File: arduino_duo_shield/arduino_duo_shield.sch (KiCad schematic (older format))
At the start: 19 parts, among them J2 Spindle_Control, J3 Motor_Control, J4 Limit_Switches, J5 Spindle_Relay_Power, J6 Spindle_Signal, P1 CONN_01X01, P10 Digital, P11 PWM, P12 PWM, P13 Communication, P2 CONN_01X01, P3 CONN_01X01, P4 CONN_01X01, P5 CONN_01X01, P6 CONN_01X01, P7 Power, P8 Analog, P9 Analog, SW1 SW_Push

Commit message: Add signal mirror and control jumpers
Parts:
- removed J2: Spindle_Control, Connector_PinHeader_2.54mm:PinHeader_1x04_P2.54mm_Vertical, symbol Connector:Conn_01x04_Male
- removed J5: Spindle_Relay_Power, TerminalBlock:TerminalBlock_bornier-2_P5.08mm, symbol Connector:Conn_01x02_Female
- removed J6: Spindle_Signal, TerminalBlock:TerminalBlock_bornier-2_P5.08mm, symbol Connector:Conn_01x02_Female
- added J2: EStop, TerminalBlock:TerminalBlock_bornier-2_P5.08mm, symbol Connector:Conn_01x02_Male
- added J5: inverter_freq, TerminalBlock:TerminalBlock_bornier-2_P5.08mm, symbol Connector:Conn_01x02_Male
- added J6: inverter_cmd, TerminalBlock:TerminalBlock_bornier-2_P5.08mm, symbol Connector:Conn_01x02_Male
- added J8: inverter_power, TerminalBlock:TerminalBlock_bornier-2_P5.08mm, symbol Connector:Conn_01x02_Male
- added J9: Motor_Control_Mirror, Connector_PinHeader_2.54mm:PinHeader_2x12_P2.54mm_Vertical, symbol Connector_Generic:Conn_02x12_Odd_Even
- J4: footprint Connector_PinHeader_2.54mm:PinHeader_2x07_P2.54mm_Vertical -> Connector_PinHeader_2.54mm:PinHeader_2x09_P2.54mm_Vertical; symbol Connector_Generic:Conn_01x14 -> Connector_Generic:Conn_01x18
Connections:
- net labels added: Amn, Amx, spdir
- wire segments 199 -> 275
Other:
- moved on the sheet: J3, SW1

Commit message: Route all paths
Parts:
- removed P1, P2, P3, P4, P5, P6: CONN_01X01, Socket_Arduino_Mega:Arduino_1pin, symbol Connector_Generic:Conn_01x01
- J2: symbol Connector:Conn_01x02_Male -> Connector:Conn_01x02_Female
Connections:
- net Spindle_VFD_Control/inverter_frequency_10V: now also J5.1 (Pin_1)
- no-connect marks 62 -> 53
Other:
- note removed: "Holes"
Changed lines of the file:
@@
 $Descr A4 11693 8268
 encoding utf-8
-Sheet 1 5
+Sheet 1 4
 Title ""
 Date "mar. 31 mars 2015"
@@
 Text Label 3000 2300 0    60   ~ 0
 AREF
-Text Notes 1600 7400 0    60   ~ 0
-Holes
-$Comp
-L Connector_Generic:Conn_01x01 P1
-U 1 1 56D70B71
-P 1500 7050
-F 0 "P1" V 1600 7050 31  0000 C CNN
-F 1 "CONN_01X01" V 1600 7050 50  0001 C CNN
-F 2 "Socket_Arduino_Mega:Arduino_1pin" H 1500 7050 50  0001 C CNN
-F 3 "" H 1500 7050 50  0000 C CNN
-	1    1500 7050
-	0    -1   -1   0
-$EndComp
-$Comp
-L Connector_Generic:Conn_01x01 P2
-U 1 1 56D70C9B
-P 1600 7050
-F 0 "P2" V 1700 7050 31  0000 C CNN
-F 1 "CONN_01X01" V 1700 7050 50  0001 C CNN
-F 2 "Socket_Arduino_Mega:Arduino_1pin" H 1600 7050 50  0001 C CNN
-F 3 "" H 1600 7050 50  0000 C CNN
-	1    1600 7050
-	0    -1   -1   0
-$EndComp
-$Comp
-L Connector_Generic:Conn_01x01 P3
-U 1 1 56D70CE6
-P 1700 7050
-F 0 "P3" V 1800 7050 31  0000 C CNN
-F 1 "CONN_01X01" V 1800 7050 50  0001 C CNN
-F 2 "Socket_Arduino_Mega:Arduino_1pin" H 1700 7050 50  0001 C CNN
-F 3 "" H 1700 7050 50  0000 C CNN
-	1    1700 7050
-	0    -1   -1   0
-$EndComp
-$Comp
-L Connector_Generic:Conn_01x01 P4
-U 1 1 56D70D2C
-P 1800 7050
-F 0 "P4" V 1900 7050 31  0000 C CNN
-F 1 "CONN_01X01" V 1900 7050 50  0001 C CNN
-F 2 "Socket_Arduino_Mega:Arduino_1pin" H 1800 7050 50  0001 C CNN
-F 3 "" H 1800 7050 50  0000 C CNN
-	1    1800 7050
-	0    -1   -1   0
-$EndComp
-$Comp
-L Connector_Generic:Conn_01x01 P5
-U 1 1 56D711A2
-P 1900 7050
-F 0 "P5" V 2000 7050 31  0000 C CNN
-F 1 "CONN_01X01" V 2000 7050 50  0001 C CNN
-F 2 "Socket_Arduino_Mega:Arduino_1pin" H 1900 7050 50  0001 C CNN
-F 3 "" H 1900 7050 50  0000 C CNN
-	1    1900 7050
-	0    -1   -1   0
-$EndComp
-$Comp
-L Connector_Generic:Conn_01x01 P6
-U 1 1 56D711F0
-P 2000 7050
-F 0 "P6" V 2100 7050 31  0000 C CNN
-F 1 "CONN_01X01" V 2100 7050 50  0001 C CNN
-F 2 "Socket_Arduino_Mega:Arduino_1pin" H 2000 7050 50  0001 C CNN
-F 3 "" H 2000 7050 50  0000 C CNN
-	1    2000 7050
-	0    -1   -1   0
-$EndComp
-NoConn ~ 1500 7250
-NoConn ~ 1600 7250
-NoConn ~ 1700 7250
-NoConn ~ 1800 7250
-NoConn ~ 1900 7250
-NoConn ~ 2000 7250
 $Comp
 L conn_01x08_arduino_power:Conn_01x08_arduino_power P7
@@
 $EndComp
 Wire Wire Line
-	7800 5550 8150 5550
-Wire Wire Line
 	5100 5900 4350 5900
 Wire Wire Line
@@
 Text Label 4100 1250 0    50   ~ 0
 VREF+
-$Sheet
-S 8150 5350 750  500
-U 5D7DFDC0
-F0 "Spindle_Power_Control" 50
-F1 "Spindle_Power_Control.sch" 50
-F2 "ext_gnd" I L 8150 5750 50
-F3 "ext_sppwm" I L 8150 5550 50
-F4 "ext_vcc" I L 8150 5650 50
-F5 "ext_spenab" I L 8150 5450 50
-$EndSheet
 Wire Wire Line
 	4350 1250 6900 1250
@@
 Wire Wire Line
 	4350 5800 4350 1250
-Wire Wire Line
-	7800 5450 8150 5450
 Wire Wire Line
 	1700 1250 4350 1250
@@
 Wire Wire Line
 	1200 3050 1850 3050
-Wire Wire Line
-	1200 2500 1950 2500
 $Comp
 L power:PWR_FLAG #FLG0104
@@
 Wire Wire Line
 	11100 5950 11100 6200
-Connection ~ 1950 2500
-Wire Wire Line
-	1950 2500 2200 2500
 Wire Wire Line
 	1850 3050 2100 3050
 $Comp
-L Connector:Conn_01x02_Male J2
+L Connector:Conn_01x02_Female J2
 U 1 1 5E163504
 P 750 3300
-F 0 "J2" V 904 3112 50  0000 R CNN
-F 1 "EStop" V 813 3112 50  0000 R CNN
+F 0 "J2" V 750 3150 50  0000 R CNN
+F 1 "EStop" V 650 3150 50  0000 R CNN
 F 2 "TerminalBlock:TerminalBlock_bornier-2_P5.08mm" H 750 3300 50  0001 C CNN
 F 3 "~" H 750 3300 50  0001 C CNN
 	1    750  3300
-	0    -1   -1   0
+	0    -1   1    0
 $EndComp
 Wire Wire Line
@@
 	6600 5450 6850 5450
 Wire Wire Line
-	6600 5350 6850 5350
+	6600 5350 6750 5350
 Wire Wire Line
 	6600 5550 6850 5550
-NoConn ~ 6850 5250
 $Comp
 L Connector:Conn_01x02_Male J?
@@
 Wire Wire Line
 	6700 3900 7000 3900
-NoConn ~ 7800 5450
-NoConn ~ 7800 5550
+Wire Wire Line
+	1200 2500 1950 2500
+Wire Wire Line
+	6850 5250 6750 5250
+Wire Wire Line
+	6750 5250 6750 5350
+Connection ~ 6750 5350
+Wire Wire Line
+	6750 5350 6850 5350
 $EndSCHEMATC

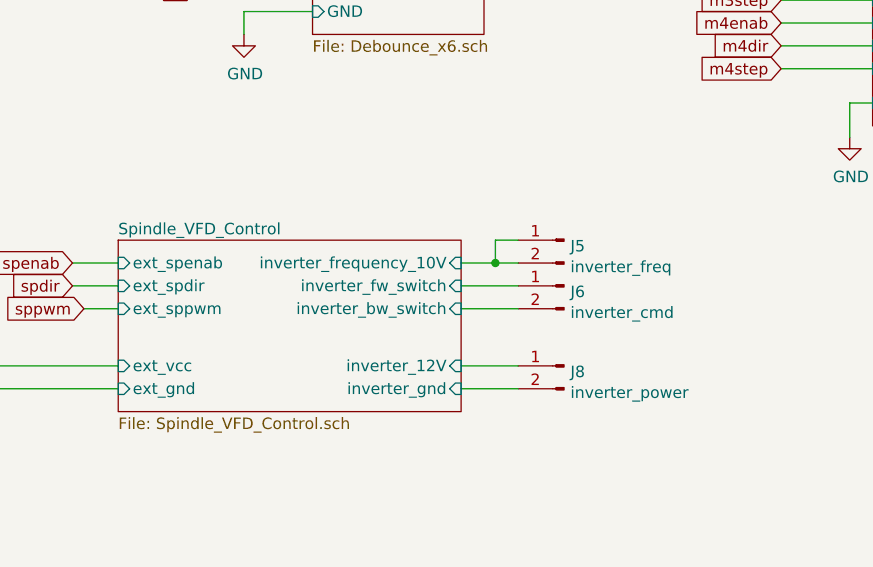
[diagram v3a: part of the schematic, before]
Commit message: Expose raw analog frequency control
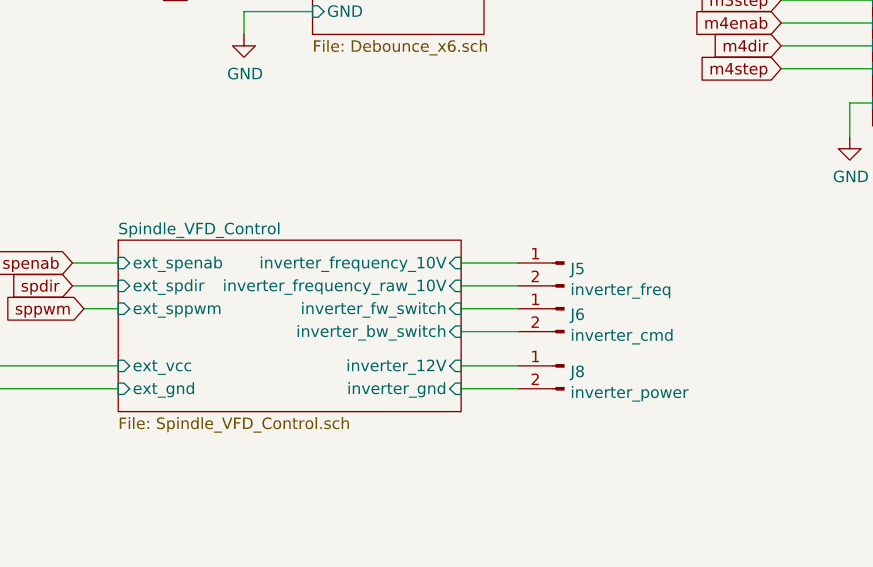
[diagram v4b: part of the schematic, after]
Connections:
- net Spindle_VFD_Control/inverter_frequency_10V: no longer J5.2 (Pin_2)
- new net Spindle_VFD_Control/inverter_frequency_raw_10V: J5.2 (Pin_2)
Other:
- moved on the sheet: J5, J6
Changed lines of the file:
@@
 F7 "ext_vcc" I L 5100 5800 50
 F8 "ext_spenab" I L 5100 5350 50
-F9 "inverter_fw_switch" I R 6600 5450 50
-F10 "inverter_bw_switch" I R 6600 5550 50
+F9 "inverter_fw_switch" I R 6600 5550 50
+F10 "inverter_bw_switch" I R 6600 5650 50
 F11 "inverter_gnd" I R 6600 5900 50
+F12 "inverter_frequency_raw_10V" I R 6600 5450 50
 $EndSheet
 Text GLabel 3450 2500 2    50   Output ~ 0
@@
 $EndComp
 Wire Wire Line
-	6600 5450 6850 5450
-Wire Wire Line
-	6600 5350 6750 5350
-Wire Wire Line
 	6600 5550 6850 5550
+Wire Wire Line
+	6600 5650 6850 5650
 $Comp
 L Connector:Conn_01x02_Male J?
 U 1 1 5E2CBC81
-P 7050 5250
+P 7050 5350
 AR Path="/5D7DFDC0/5E2CBC81" Ref="J?"  Part="1"
 AR Path="/5E2CBC81" Ref="J5"  Part="1"
-F 0 "J5" H 7022 5224 50  0000 R CNN
-F 1 "inverter_freq" H 7022 5133 50  0000 R CNN
-F 2 "TerminalBlock:TerminalBlock_bornier-2_P5.08mm" H 7050 5250 50  0001 C CNN
-F 3 "~" H 7050 5250 50  0001 C CNN
-	1    7050 5250
+F 0 "J5" H 7022 5324 50  0000 R CNN
+F 1 "inverter_freq" H 7022 5233 50  0000 R CNN
+F 2 "TerminalBlock:TerminalBlock_bornier-2_P5.08mm" H 7050 5350 50  0001 C CNN
+F 3 "~" H 7050 5350 50  0001 C CNN
+	1    7050 5350
 	-1   0    0    -1
 $EndComp
@@
 L Connector:Conn_01x02_Male J?
 U 1 1 5E2B9818
-P 7050 5450
+P 7050 5550
 AR Path="/5D7DFDC0/5E2B9818" Ref="J?"  Part="1"
 AR Path="/5E2B9818" Ref="J6"  Part="1"
-F 0 "J6" H 7022 5424 50  0000 R CNN
-F 1 "inverter_cmd" H 7022 5333 50  0000 R CNN
-F 2 "TerminalBlock:TerminalBlock_bornier-2_P5.08mm" H 7050 5450 50  0001 C CNN
-F 3 "~" H 7050 5450 50  0001 C CNN
-	1    7050 5450
+F 0 "J6" H 7022 5524 50  0000 R CNN
+F 1 "inverter_cmd" H 7022 5433 50  0000 R CNN
+F 2 "TerminalBlock:TerminalBlock_bornier-2_P5.08mm" H 7050 5550 50  0001 C CNN
+F 3 "~" H 7050 5550 50  0001 C CNN
+	1    7050 5550
 	-1   0    0    -1
 $EndComp
@@
 	1200 2500 1950 2500
 Wire Wire Line
-	6850 5250 6750 5250
-Wire Wire Line
-	6750 5250 6750 5350
-Connection ~ 6750 5350
-Wire Wire Line
-	6750 5350 6850 5350
+	6850 5350 6600 5350
 Wire Wire Line
 	6600 5900 6850 5900
 Wire Wire Line
 	6600 5800 6850 5800
+Wire Wire Line
+	6600 5450 6850 5450
 $EndSCHEMATC
